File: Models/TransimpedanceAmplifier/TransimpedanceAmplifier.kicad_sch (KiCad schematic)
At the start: 3 parts, among them J1 Conn_01x02_Socket, J2 Conn_01x02_Socket, J3 Conn_01x03_Pin

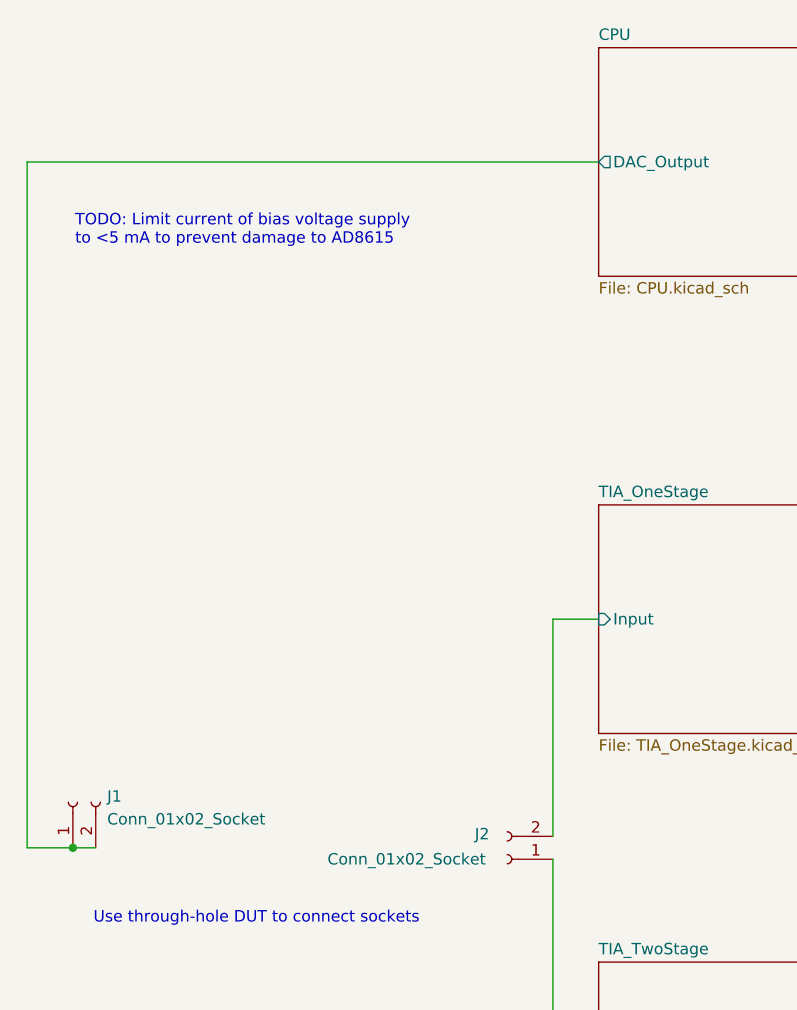
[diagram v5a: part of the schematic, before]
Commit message: Resolved input overvoltage protection for AD8615 and DAC
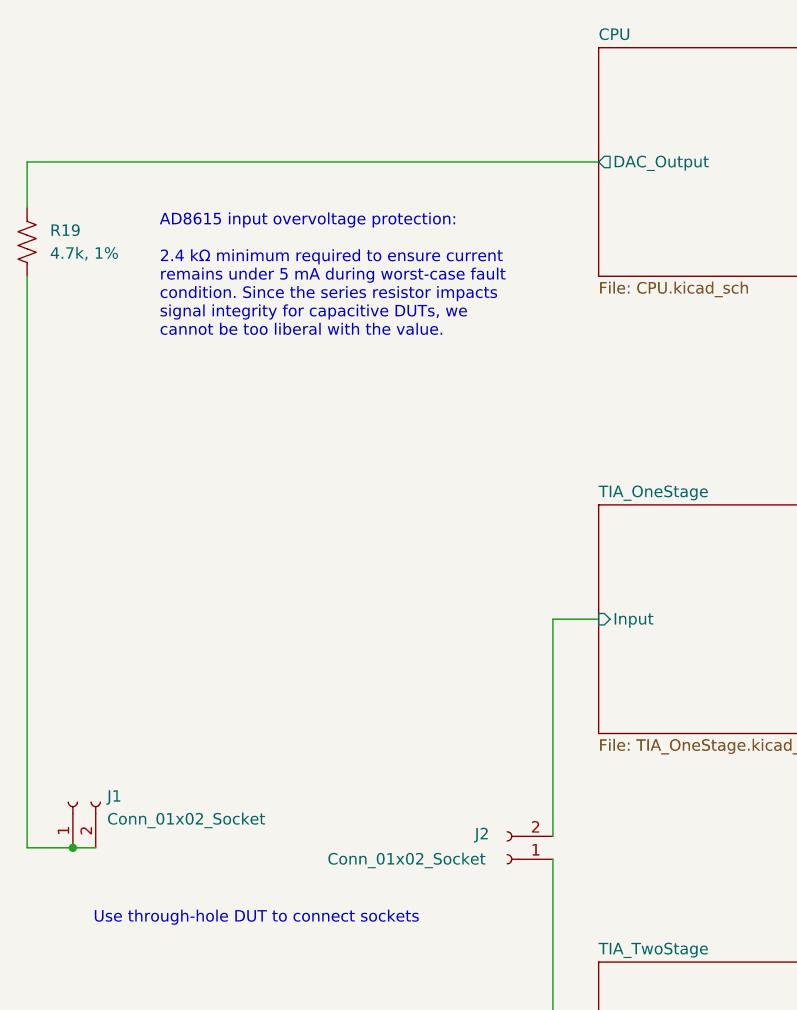
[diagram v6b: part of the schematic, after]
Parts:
- added R19: 4.7k, 1%, symbol Device:R_US
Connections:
- net CPU/DAC_Output: now also R19.1; no longer J1.1 (Pin_1), J1.2 (Pin_2)
- new net: J1.1 (Pin_1), J1.2 (Pin_2), R19.2
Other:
- note added: "AD8615 input overvoltage protection: 2.4 kΩ minimum required to ensure current remains under 5 mA during worst-case fault condition. Since the series resistor impacts signal integrity for capacitive DUTs, we cannot be too liberal with the value."
- note removed: "TODO: Limit current of bias voltage supply to <5 mA to prevent damage to AD8615"
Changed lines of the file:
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@@
 		)
 	)
-	(text "TODO: Limit current of bias voltage supply\nto <5 mA to prevent damage to AD8615"
+	(text "AD8615 input overvoltage protection:\n\n2.4 kΩ minimum required to ensure current\nremains under 5 mA during worst-case fault\ncondition. Since the series resistor impacts\nsignal integrity for capacitive DUTs, we\ncannot be too liberal with the value."
 		(exclude_from_sim no)
-		(at 45.974 51.562 0)
+		(at 55.372 51.562 0)
 		(effects
 			(font
@@
 	(wire
 		(pts
+			(xy 40.64 58.42) (xy 40.64 121.92)
+		)
+		(stroke
+			(width 0)
+			(type default)
+		)
+	)
+	(wire
+		(pts
 			(xy 99.06 96.52) (xy 104.14 96.52)
 		)
@@
 	(wire
 		(pts
+			(xy 40.64 45.72) (xy 40.64 50.8)
+		)
+		(stroke
+			(width 0)
+			(type default)
+		)
+	)
+	(wire
+		(pts
 			(xy 144.78 45.72) (xy 172.72 45.72)
 		)
@@
 		(pts
 			(xy 45.72 121.92) (xy 48.26 121.92)
-		)
-		(stroke
-			(width 0)
-			(type default)
-		)
-	)
-	(wire
-		(pts
-			(xy 40.64 121.92) (xy 40.64 45.72)
 		)
 		(stroke
@@
 					(unit 1)
 				)
+			)
+		)
+	)
+	(symbol
+		(lib_id "Device:R_US")
+		(at 40.64 54.61 0)
+		(unit 1)
+		(exclude_from_sim no)
+		(in_bom yes)
+		(on_board yes)
+		(dnp no)
+		(fields_autoplaced yes)
+		(property "Reference" "R19"
+			(at 43.18 53.3399 0)
+			(effects
+				(font
+					(size 1.27 1.27)
+				)
+				(justify left)
+			)
+		)
+		(property "Value" "4.7k, 1%"
+			(at 43.18 55.8799 0)
+			(effects
+				(font
+					(size 1.27 1.27)
+				)
+				(justify left)
+			)
+		)
+		(property "Footprint" ""
+			(at 41.656 54.864 90)
+			(effects
+				(font
+					(size 1.27 1.27)
+				)
+				(hide yes)
+			)
+		)
+		(property "Datasheet" "~"
+			(at 40.64 54.61 0)
+			(effects
+				(font
+					(size 1.27 1.27)
+				)
+				(hide yes)
+			)
+		)
+		(property "Description" "Resistor, US symbol"
+			(at 40.64 54.61 0)
+			(effects
+				(font
+					(size 1.27 1.27)
+				)
+				(hide yes)
+			)
+		)
+		(property "Purchase Link" "https://www.digikey.com/en/products/detail/vishay-dale/CRCW06034K70FKEA/1174744"
+			(at 40.64 54.61 0)
+			(effects
+				(font
+					(size 1.27 1.27)
+				)
+				(hide yes)
+			)
+		)
+		(pin "1"
+		)
+		(pin "2"
+		)
+		(instances
+			(project ""
+				(path "/ec9f2ae3-e40d-40eb-9760-2b611ee8efd1"
+					(reference "R19")
+					(unit 1)
+				)

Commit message: Finalized the last detail of the schematic
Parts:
- renumbered R19 to R1
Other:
- note added: "Use through-hole DUT to connect sockets Specification of DUTs is out of scope for the KiCad schematic"
- note removed: "Use through-hole DUT to connect sockets"
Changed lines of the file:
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@@
 		)
 	)
-	(text "Use through-hole DUT to connect sockets"
+	(text "Use through-hole DUT to connect sockets\n\nSpecification of DUTs is out of scope for\nthe KiCad schematic"
 		(exclude_from_sim no)
 		(at 48.006 129.032 0)
@@
 		(dnp no)
 		(fields_autoplaced yes)
-		(property "Reference" "R19"
+		(property "Reference" "R1"
 			(at 43.18 53.3399 0)
 			(effects
@@
 			(project ""
 				(path "/ec9f2ae3-e40d-40eb-9760-2b611ee8efd1"
-					(reference "R19")
+					(reference "R1")
 					(unit 1)
 				)

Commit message: Working on filling in the last details of the schematics
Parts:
- J1, J2: footprint (none) -> Connector_Custom:PinSocket_1x2; Cost (none) -> $0.00; RoHS Compliant (none) -> NO
- J3: footprint (none) -> Connector_Custom:PinHeader_1x3; Cost (none) -> $0.00; RoHS Compliant (none) -> NO
- R1: Cost (none) -> $0.00; RoHS Compliant (none) -> NO
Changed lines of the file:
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@@
 			)
 		)
-		(property "Footprint" ""
+		(property "Footprint" "Connector_Custom:PinSocket_1x2"
 			(at 93.98 123.19 0)
 			(effects
@@
 		)
 		(property "Purchase Link" "https://www.digikey.com/en/products/detail/sullins-connector-solutions/PPPC021LFBN-RC/810174"
+			(at 93.98 123.19 0)
+			(effects
+				(font
+					(size 1.27 1.27)
+				)
+				(hide yes)
+			)
+		)
+		(property "Cost" "$0.00"
+			(at 93.98 123.19 0)
+			(effects
+				(font
+					(size 1.27 1.27)
+				)
+				(hide yes)
+			)
+		)
+		(property "RoHS Compliant" "NO"
 			(at 93.98 123.19 0)
 			(effects
@@
 			)
 		)
-		(property "Footprint" ""
+		(property "Footprint" "Connector_Custom:PinHeader_1x3"
 			(at 160.02 121.92 0)
 			(effects
@@
 		)
 		(property "Purchase Link" "https://www.digikey.com/en/products/detail/sullins-connector-solutions/QPC02SXGN-RC/2618262"
+			(at 160.02 121.92 0)
+			(effects
+				(font
+					(size 1.27 1.27)
+				)
+				(hide yes)
+			)
+		)
+		(property "Cost" "$0.00"
+			(at 160.02 121.92 0)
+			(effects
+				(font
+					(size 1.27 1.27)
+				)
+				(hide yes)
+			)
+		)
+		(property "RoHS Compliant" "NO"
 			(at 160.02 121.92 0)
 			(effects
@@
 			)
 		)
+		(property "Cost" "$0.00"
+			(at 40.64 54.61 0)
+			(effects
+				(font
+					(size 1.27 1.27)
+				)
+				(hide yes)
+			)
+		)
+		(property "RoHS Compliant" "NO"
+			(at 40.64 54.61 0)
+			(effects
+				(font
+					(size 1.27 1.27)
+				)
+				(hide yes)
+			)
+		)
 		(pin "1"
 		)
@@
 			)
 		)
-		(property "Footprint" ""
+		(property "Footprint" "Connector_Custom:PinSocket_1x2"
 			(at 45.72 116.84 0)
 			(effects
@@
 			(at 45.72 116.84 90)
 			(effects
+				(font
+					(size 1.27 1.27)
+				)
+				(hide yes)
+			)
+		)
+		(property "Cost" "$0.00"
+			(at 45.72 116.84 90)
+			(effects
+				(font
+					(size 1.27 1.27)
+				)
+				(hide yes)
+			)
+		)
+		(property "RoHS Compliant" "NO"
+			(at 45.72 116.84 90)
+			(effects
